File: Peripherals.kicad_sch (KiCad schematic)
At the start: 19 parts, among them J402 SD port, SW400 Mode Switch, SW401 Reset, U400 AT25DF321A-SH-T

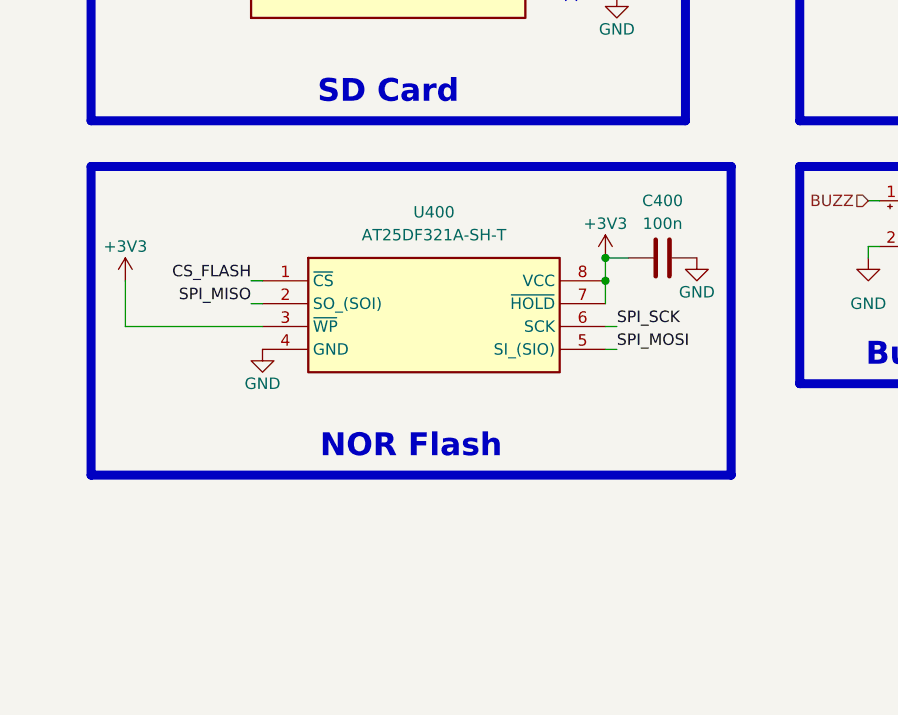
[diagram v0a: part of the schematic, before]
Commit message: [PCB][Fixed] Fixed wrong Diode footprint and Changed TVS diode package, also changed wrong footprint of CAN transiever chip. [Changed] Changed the FLASH chip to a different model due to a stocking issue
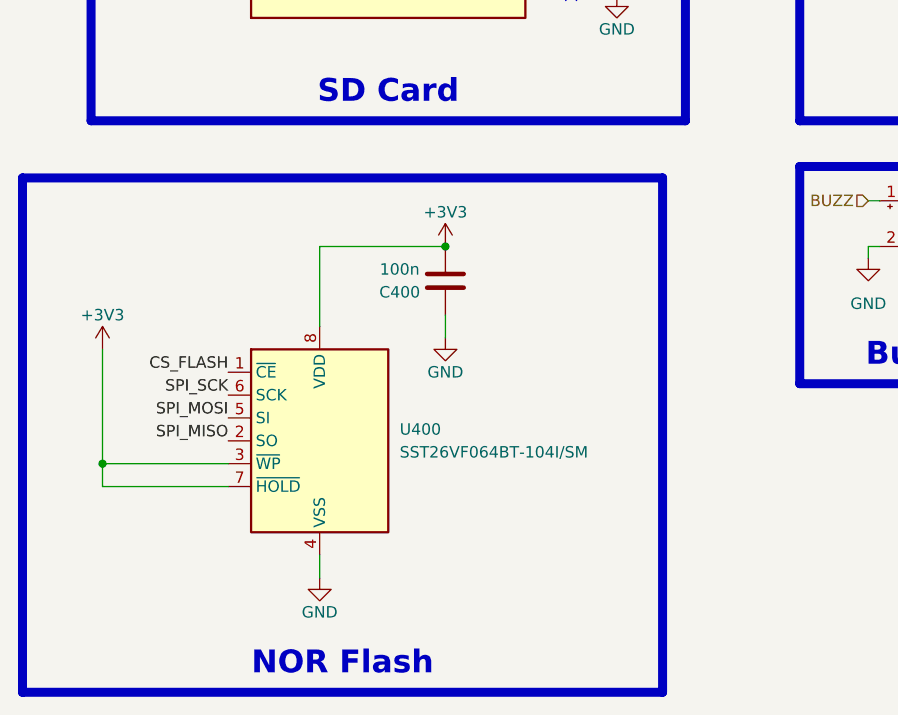
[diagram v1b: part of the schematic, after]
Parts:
- removed U400: AT25DF321A-SH-T, Package_SO:SOIC-8_3.9x4.9mm_P1.27mm, symbol AT25DF321A-SH-T:AT25DF321A-SH-T
- added U400: SST26VF064BT-104I/SM, Package_SO:SOIC-8_5.3x5.3mm_P1.27mm, symbol Memory_Flash:SST25VF080B-50-4x-S2Ax
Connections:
- net +3V3: now also C400.1, U400.3 (~{WP}), U400.7 (~{HOLD}), U400.8 (VDD); no longer C400.2
- net CS_FLASH: now also U400.1 (~{CE})
- net GND: now also C400.2, U400.4 (VSS); no longer C400.1
- net SPI_MISO: now also U400.2 (SO)
- net SPI_MOSI: now also U400.5 (SI)
- net SPI_SCK: now also U400.6 (SCK)
